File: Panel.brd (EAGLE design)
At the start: 100 x 100 mm, 42 parts, among them IC1 74HCT04D, U1 TPIC6B595N, U2 TPIC6B595N, U3 TPIC6B595N, U4 TPIC6B595N, U5 TPIC6B595N, U6 TPIC6B595N, U7 CJT1117-3.3-SOT223

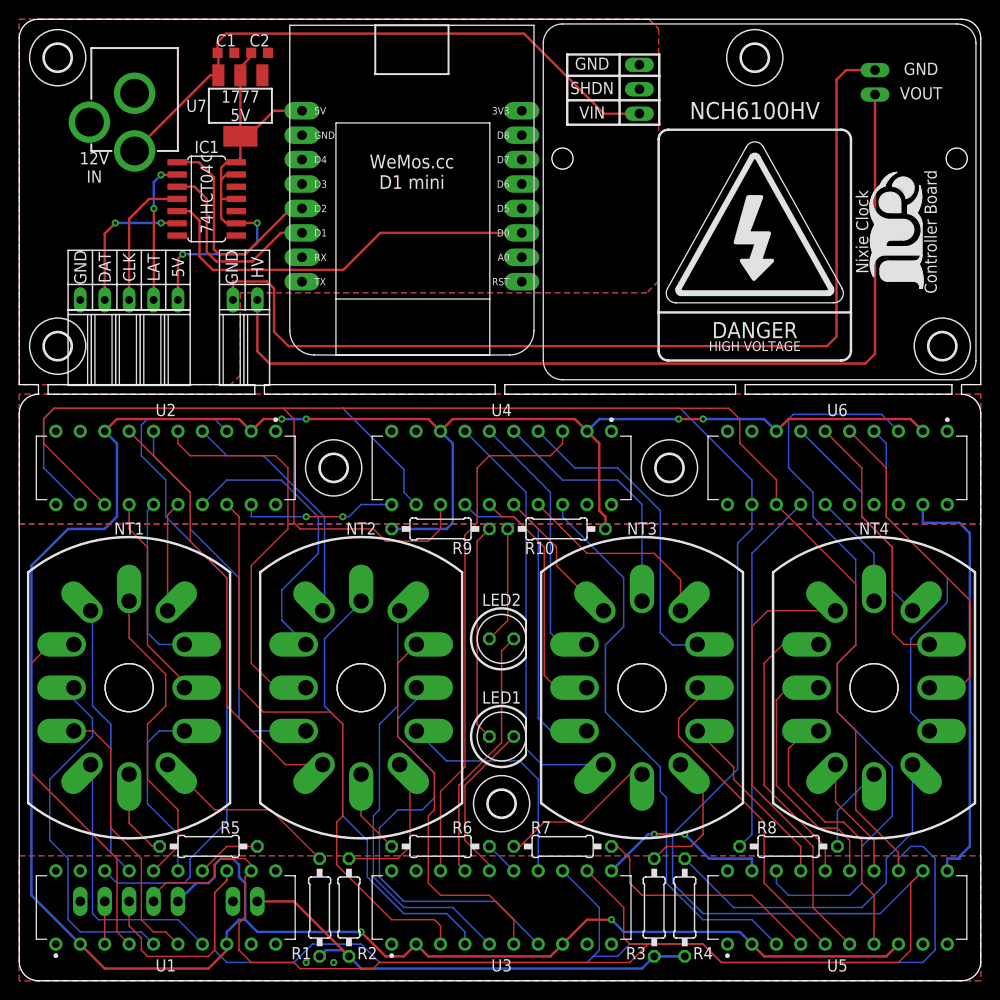
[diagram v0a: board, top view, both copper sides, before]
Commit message: fixed airwire in front panel and updated panel
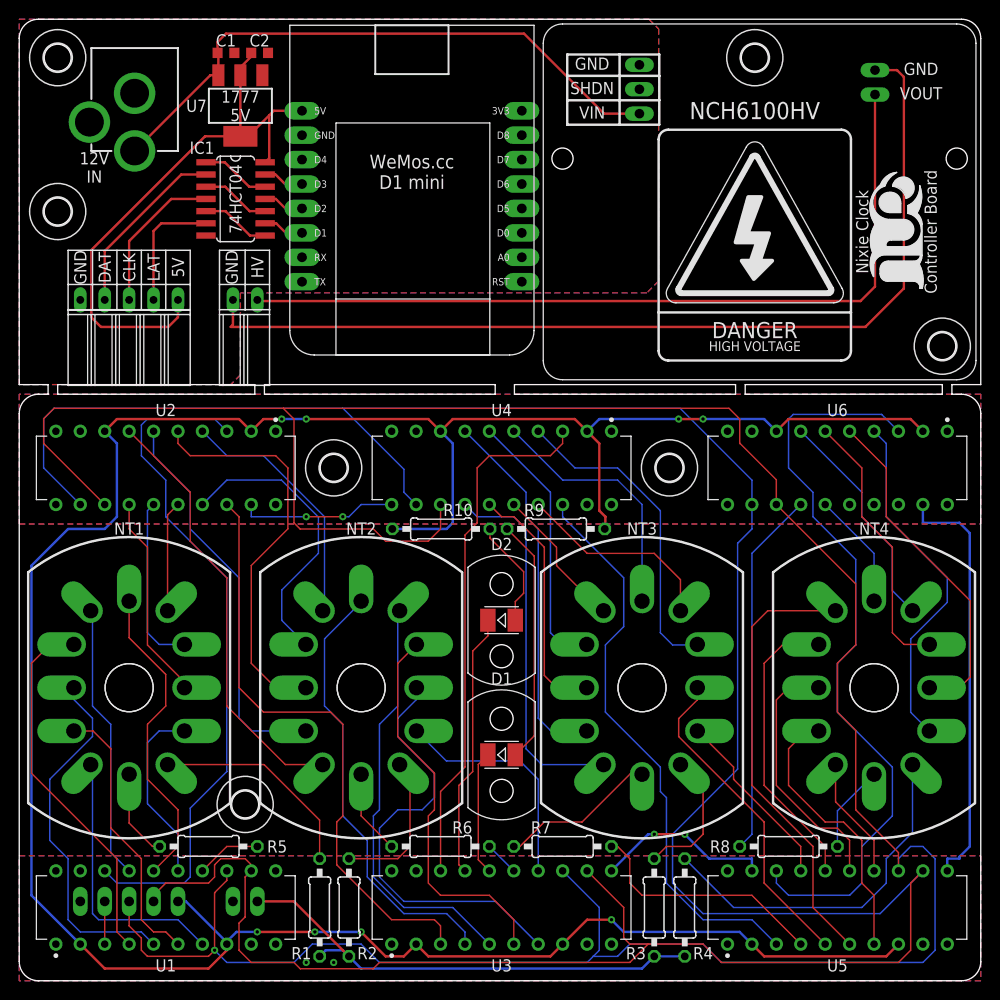
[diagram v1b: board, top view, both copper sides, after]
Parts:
- removed LED1, LED2: (no value), led:LED5MM
- added D1, D2: (no value), Wurth_Elektronik_Optoelectronics_rev17b:WL-SMTW_3528
- added U$13, U$14: (no value), holes:2,8
- U$5: value NCH6100HV -> (none); device NixieClock:NCH6100HV -> NixieClock:MENTOR-1216.1005
- U$6: device OwnStuff:LOGO-SILKSCREEN -> NixieClock:MENTOR-1216.1005
- U$7: value (none) -> NCH6100HV; device holes:2,8 -> NixieClock:NCH6100HV
- U$8: device holes:2,8 -> OwnStuff:LOGO-SILKSCREEN
- moved U$9 96.8 mm to (96.0, 66.0)
- moved U$8 89.0 mm to (92.2, 77.9), turned to 90 degrees
- moved U$10 74.2 mm to (4.00, 80.0)
- moved U$6 68.8 mm to (50.2, 23.5)
- moved U$5 62.2 mm to (50.2, 37.5), turned to 90 degrees
- moved U$7 53.3 mm to (54.5, 99.5)
- moved U$4 26.8 mm to (23.2, 44.2)
- moved U$3 26.7 mm to (23.5, 18.3)
- moved R10 12.0 mm to (43.9, 47.0), turned to 180 degrees
- moved R9 12.0 mm to (55.8, 47.0), turned to 0 degrees
- moved IC1 3.00 mm to (22.5, 81.3)
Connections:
- removed net GND2: C1.2, C2.2, DATA1.5, HV1.2, IC1.7, U$11.GND, U$11.GNDBREAK, U$12.GND, U$5.GND1, U$5.GND2, U7.1
- removed net N$54: DATA1.2, IC1.2
- removed net N$61: IC1.5, U$12.D0
- new net GND: DATA.1, HV.1, U1.10, U1.11, U1.19, U1.9, U2.10, U2.11, U2.19, U2.9, U3.10, U3.11, U3.19, U3.9, U4.10, U4.11, U4.19, U4.9, U5.10, U5.11, U5.19, U5.9, U6.10, U6.11, U6.19, U6.9
- new net N$2: IC1.5, IC1.8
- new net N$3: IC1.10, IC1.3
- new net N$4: IC1.1, IC1.12
- new net N$7: IC1.13, U$12.D3
- new net N$8: DATA1.4, IC1.2
- net +12V: now also U$7.VIN; no longer U$5.VIN
- net +5V1: no longer IC1.11, IC1.13, IC1.9
- net GND1: now also C1.2, C2.2, DATA1.5, HV1.2, IC1.7, U$11.GND, U$11.GNDBREAK, U$12.GND, U$7.GND1, U$7.GND2, U7.1; no longer DATA.1, HV.1, U1.10, U1.11, U1.19, U1.9, U2.10, U2.11, U2.19, U2.9, U3.10, U3.11, U3.19, U3.9, U4.10, U4.11, U4.19, U4.9, U5.10, U5.11, U5.19, U5.9, U6.10, U6.11, U6.19, U6.9
- net LED1: now also D1.1; no longer LED1.K
- net LED2: now also D2.1; no longer LED2.K
- net N$1: now also U$7.VOUT; no longer U$5.VOUT
- net N$60: now also DATA1.2; no longer DATA1.4
- net N$62: now also IC1.9; no longer IC1.3
- net N$63: now also IC1.11; no longer IC1.1
- net N$66: now also D1.2; no longer LED1.A
- net N$67: now also D2.2; no longer LED2.A
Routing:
- net GND2: track 101.6 -> 0.00 mm
- net GND: track 0.00 -> 79.0 mm, vias 0 -> 6
- net N$61: track 42.2 -> 0.00 mm
- net GND1: track 79.0 -> 99.9 mm, vias 6 -> 0
- net N$63: track 23.3 -> 4.24 mm
- net N$8: track 0.00 -> 18.9 mm
- net N$62: track 20.7 -> 4.24 mm
- net N$54: track 15.0 -> 0.00 mm, vias 2 -> 0
- net N$1: track 97.5 -> 84.9 mm
- net +5V1: track 49.5 -> 61.9 mm, vias 2 -> 0
- net +5V: track 290.7 -> 280.9 mm, vias 6 -> 8
- net SCLK: track 308.6 -> 299.8 mm, vias 0 -> 1
- net N$2: track 0.00 -> 7.20 mm
- net N$4: track 0.00 -> 7.20 mm
- net N$3: track 0.00 -> 7.20 mm
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- added copper zone on layer 1, net GND
- added copper zone on layer 16, net GND
- removed copper zone on layer 1, net GND2
- removed copper zone on layer 16, net GND2
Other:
- outline, holes or cut-outs redrawn
